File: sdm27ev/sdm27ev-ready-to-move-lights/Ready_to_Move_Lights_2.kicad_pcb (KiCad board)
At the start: 2 copper layers, 52.1 x 90.2 mm, 42 parts, among them IC1 TLV2371QDBVRQ1, J1 PET-02-XX-X-VT-LC, J2 776280-1, K1 VORA1150-X017T, Q1 IRLZ44N, U1 LM393LVQDDFRQ1, U2 PAMC0381D10QDFXRQ1, U3 NE555D

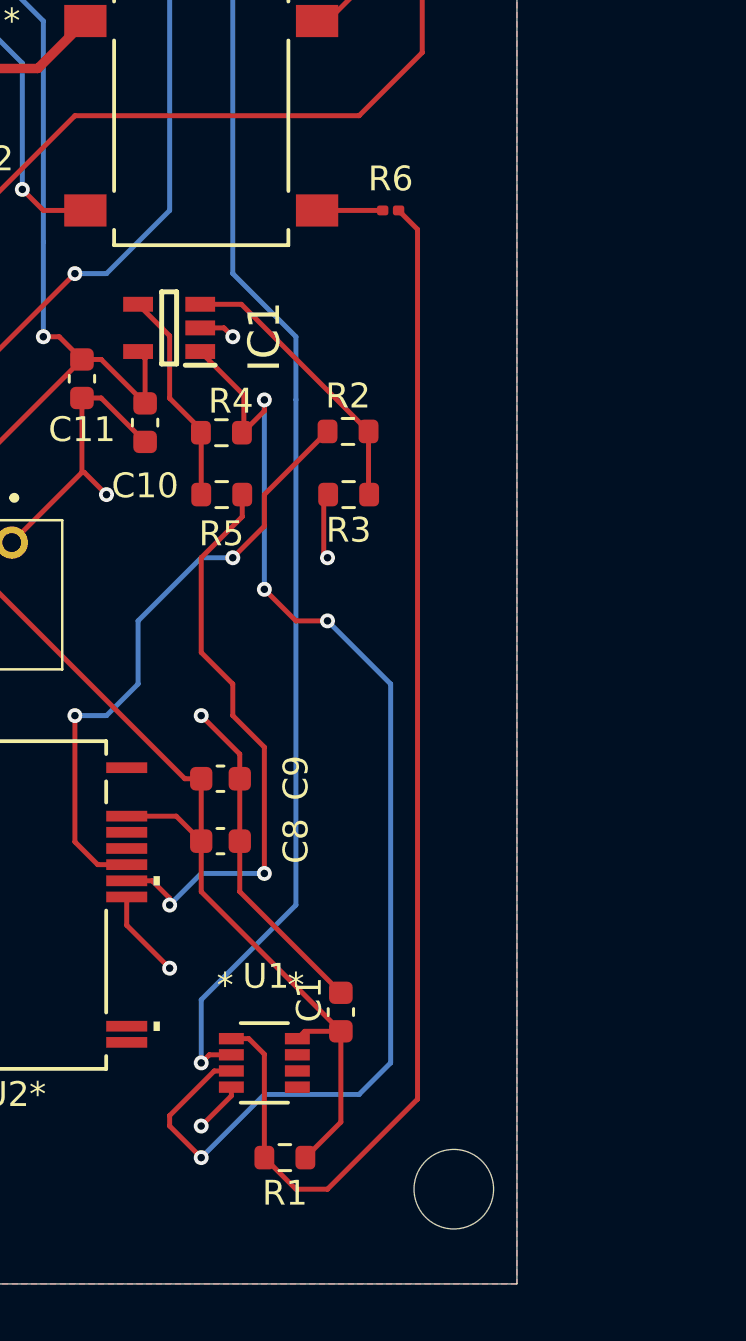
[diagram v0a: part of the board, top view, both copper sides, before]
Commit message: Fixed rtml resistor footprint + gerbers
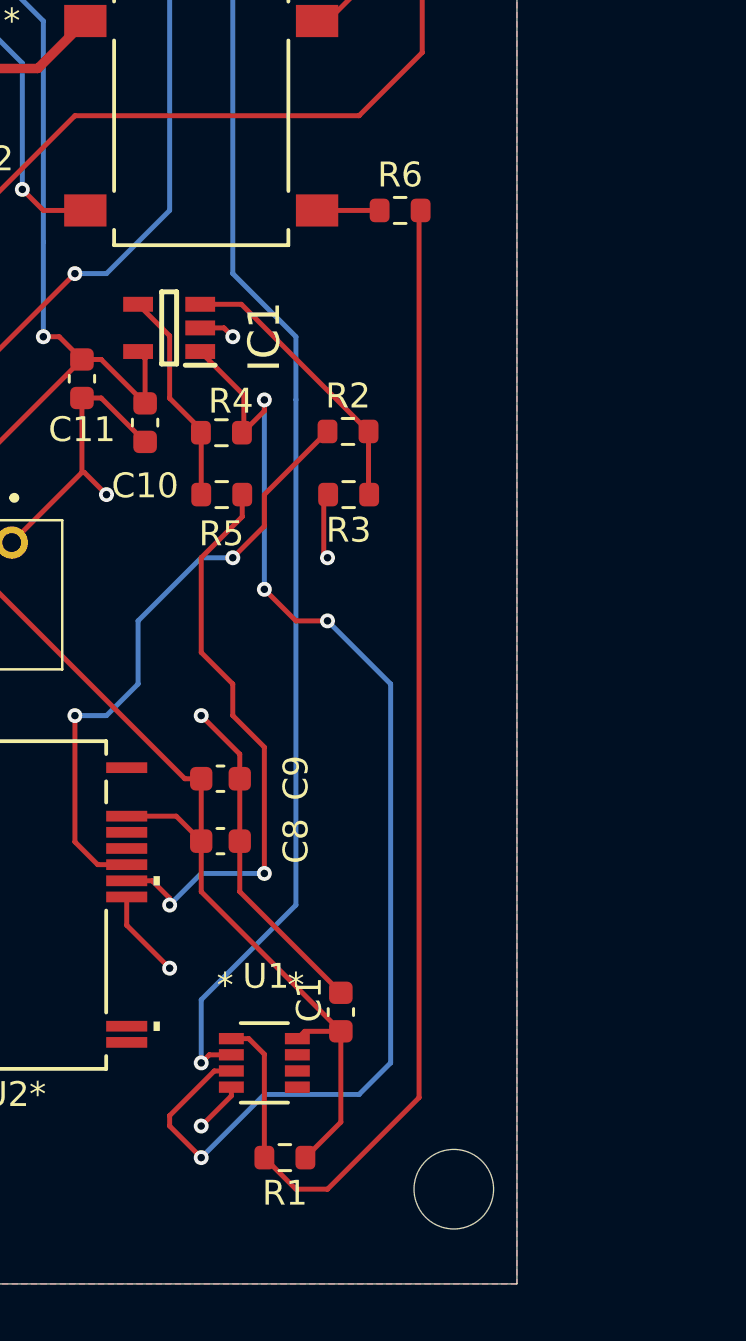
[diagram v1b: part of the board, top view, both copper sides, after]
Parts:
- R6: footprint Resistor_SMD:R_0201_0603Metric -> Resistor_SMD:R_0603_1608Metric
- moved R6 0.38 mm to (145.2, 87.6)
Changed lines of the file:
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@@
 		(embedded_fonts no)
 	)
-	(footprint "Resistor_SMD:R_0201_0603Metric"
+	(footprint "Resistor_SMD:R_0603_1608Metric"
 		(layer "F.Cu")
-		(at 144.78 87.63)
-		(descr "Resistor SMD 0201 (0603 Metric), square (rectangular) end terminal, IPC-7351 nominal, (Body size source: https://www.vishay.com/docs/20052/crcw0201e3.pdf), generated with kicad-footprint-generator")
+		(at 145.161 87.63)
+		(descr "Resistor SMD 0603 (1608 Metric), square (rectangular) end terminal, IPC-7351 nominal, (Body size source: IPC-SM-782 page 72, https://www.pcb-3d.com/wordpress/wp-content/uploads/ipc-sm-782a_amendment_1_and_2.pdf), generated with kicad-footprint-generator")
 		(tags "resistor")
 		(property "Reference" "R6"
-			(at 0 -1.27 0)
+			(at 0 -1.43 0)
 			(layer "F.SilkS")
 			(effects
@@
 		)
 		(property "Value" "1.2K"
-			(at 0 1.05 0)
+			(at 0 1.43 0)
 			(layer "F.Fab")
 			(effects
@@
 			)
 		)
-		(property "Datasheet" "~"
+		(property "Datasheet" ""
 			(at 0 0 0)
 			(layer "F.Fab")
@@
 			)
 		)
-		(property "Description" "Resistor"
+		(property "Description" ""
 			(at 0 0 0)
 			(layer "F.Fab")
@@
 		(attr smd)
 		(fp_line
-			(start -0.7 -0.35)
-			(end 0.7 -0.35)
-			(stroke
-				(width 0.05)
-				(type solid)
-			)
-			(layer "F.CrtYd")
-		)
-		(fp_line
-			(start -0.7 0.35)
-			(end -0.7 -0.35)
+			(start -0.237258 -0.5225)
+			(end 0.237258 -0.5225)
 			(stroke
-				(width 0.05)
+				(width 0.12)
 				(type solid)
 			)
-			(layer "F.CrtYd")
+			(layer "F.SilkS")
 		)
 		(fp_line
-			(start 0.7 -0.35)
-			(end 0.7 0.35)
+			(start -0.237258 0.5225)
+			(end 0.237258 0.5225)
 			(stroke
-				(width 0.05)
+				(width 0.12)
 				(type solid)
 			)
-			(layer "F.CrtYd")
+			(layer "F.SilkS")
 		)
-		(fp_line
-			(start 0.7 0.35)
-			(end -0.7 0.35)
+		(fp_rect
+			(start -1.48 -0.73)
+			(end 1.48 0.73)
 			(stroke
 				(width 0.05)
 				(type solid)
 			)
+			(fill no)
 			(layer "F.CrtYd")
 		)
-		(fp_line
-			(start -0.3 -0.15)
-			(end 0.3 -0.15)
-			(stroke
-				(width 0.1)
-				(type solid)
-			)
-			(layer "F.Fab")
-		)
-		(fp_line
-			(start -0.3 0.15)
-			(end -0.3 -0.15)
-			(stroke
-				(width 0.1)
-				(type solid)
-			)
-			(layer "F.Fab")
-		)
-		(fp_line
-			(start 0.3 -0.15)
-			(end 0.3 0.15)
-			(stroke
-				(width 0.1)
-				(type solid)
-			)
-			(layer "F.Fab")
-		)
-		(fp_line
-			(start 0.3 0.15)
-			(end -0.3 0.15)
+		(fp_rect
+			(start -0.8 -0.4125)
+			(end 0.8 0.4125)
 			(stroke
 				(width 0.1)
 				(type solid)
 			)
+			(fill no)
 			(layer "F.Fab")
 		)
 		(fp_text user "${REFERENCE}"
-			(at 0 -0.68 0)
+			(at 0 0 0)
 			(layer "F.Fab")
 			(effects
 				(font
-					(size 0.25 0.25)
-					(thickness 0.04)
+					(size 0.4 0.4)
+					(thickness 0.06)
 				)
 			)
 		)
-		(pad "" smd roundrect
-			(at -0.345 0)
-			(size 0.318 0.36)
-			(layers "F.Paste")
-			(roundrect_rratio 0.25)
-		)
-		(pad "" smd roundrect
-			(at 0.345 0)
-			(size 0.318 0.36)
-			(layers "F.Paste")
-			(roundrect_rratio 0.25)
-		)
 		(pad "1" smd roundrect
-			(at -0.32 0)
-			(size 0.46 0.4)
-			(layers "F.Cu" "F.Mask")
+			(at -0.825 0)
+			(size 0.8 0.95)
+			(layers "F.Cu" "F.Mask" "F.Paste")
 			(roundrect_rratio 0.25)
 			(net 21 "Net-(K1-Pad1)")
@@
 		)
 		(pad "2" smd roundrect
-			(at 0.32 0)
-			(size 0.46 0.4)
-			(layers "F.Cu" "F.Mask")
+			(at 0.825 0)
+			(size 0.8 0.95)
+			(layers "F.Cu" "F.Mask" "F.Paste")
 			(roundrect_rratio 0.25)
 			(net 17 "/V_IND")
@@
 		)
 		(embedded_fonts no)
-		(model "${KICAD9_3DMODEL_DIR}/Resistor_SMD.3dshapes/R_0201_0603Metric.step"
+		(model "${KICAD9_3DMODEL_DIR}/Resistor_SMD.3dshapes/R_0603_1608Metric.step"
 			(offset
 				(xyz 0 0 0)
@@
 	)
 	(segment
-		(start 145.861 123.379)
-		(end 142.24 127)
-		(width 0.2)
-		(layer "F.Cu")
-		(net 17)
-	)
-	(segment
 		(start 139.7 121.570521)
 		(end 139.0745 120.945021)
@@
 	)
 	(segment
-		(start 140.97 127)
-		(end 139.7 125.73)
+		(start 145.923 87.693)
+		(end 145.923 123.317)
 		(width 0.2)
 		(layer "F.Cu")
@@
 	)
 	(segment
-		(start 142.24 127)
-		(end 140.97 127)
+		(start 145.923 123.317)
+		(end 142.24 127)
 		(width 0.2)
 		(layer "F.Cu")
@@
 	)
 	(segment
-		(start 145.1 87.63)
-		(end 145.861 88.391)
+		(start 145.986 87.63)
+		(end 145.923 87.693)
 		(width 0.2)
 		(layer "F.Cu")
@@
 	)
 	(segment
-		(start 145.861 88.391)
-		(end 145.861 123.379)
+		(start 142.24 127)
+		(end 140.97 127)
+		(width 0.2)
+		(layer "F.Cu")
+		(net 17)
+	)
+	(segment
+		(start 140.97 127)
+		(end 139.7 125.73)
 		(width 0.2)
 		(layer "F.Cu")
@@
 	)
 	(segment
-		(start 144.46 87.63)
+		(start 144.336 87.63)
 		(end 141.8209 87.63)
 		(width 0.2)
